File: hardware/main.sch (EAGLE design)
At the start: 97 parts, among them IC1 MPU-6050, IC2 TB6612FNG, Q1 TEFT4300, Q2 TEFT4300, Q3 TEFT4300, Q4 TEFT4300, Q5 TEFT4300, Q6 TEFT4300, Q7 IRLML2244, Q9 IRLML2244, T1 IRLML0030, T2 IRLML0030, T3 IRLML0030, T4 IRLML0030, T5 IRLML0030, T6 IRLML0030, T8 IRLML0030

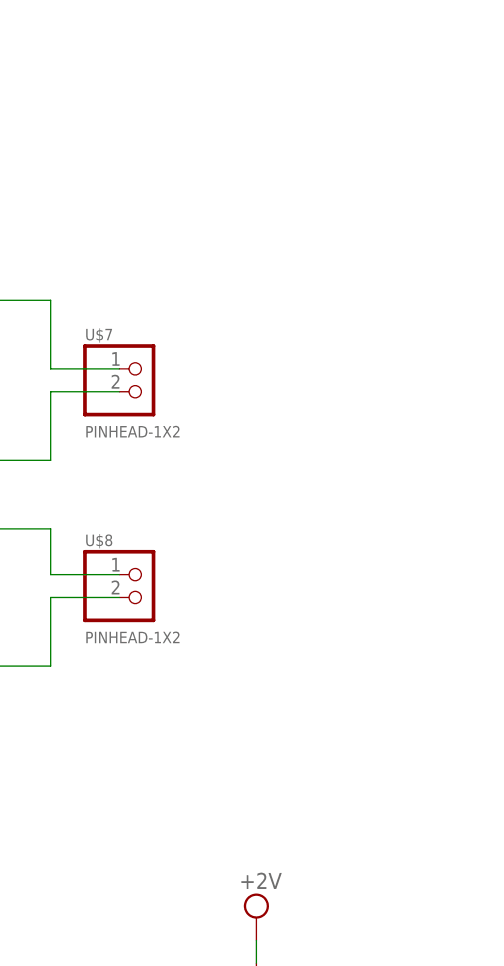
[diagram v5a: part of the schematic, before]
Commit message: added led_mount to model, pcb elemets grouped
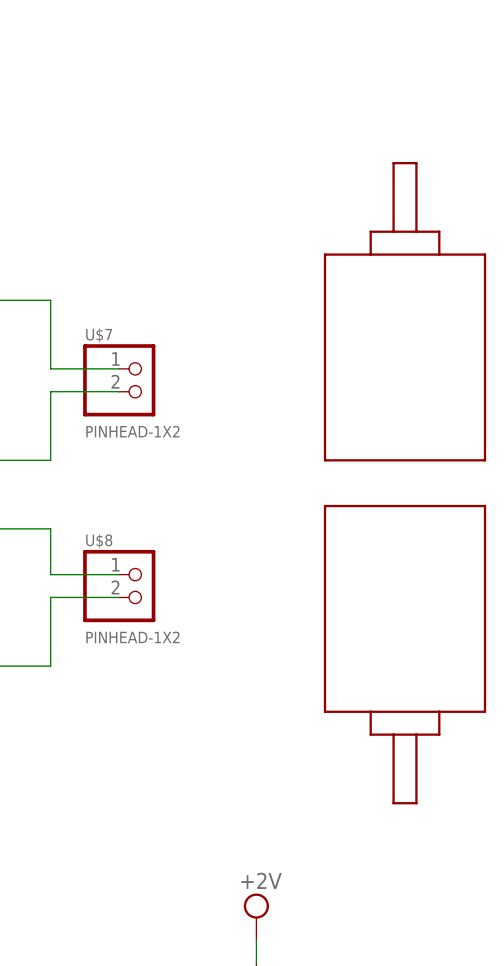
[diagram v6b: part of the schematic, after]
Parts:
- added M1: MOTOR_MOUNT_V2, micromouse:MOTOR_MOUNT_V2
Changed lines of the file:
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@@
 <?xml version="1.0" encoding="utf-8"?>
 <!DOCTYPE eagle SYSTEM "eagle.dtd">
-<eagle version="7.7.0">
+<eagle version="8.0.0">
 <drawing>
 <settings>
@@
 <grid distance="0.1" unitdist="inch" unit="inch" style="lines" multiple="1" display="no" altdistance="0.01" altunitdist="inch" altunit="inch"/>
 <layers>
-<layer number="1" name="Top" color="4" fill="1" visible="yes" active="no"/>
-<layer number="2" name="Route2" color="1" fill="3" visible="yes" active="no"/>
-<layer number="3" name="Route3" color="4" fill="3" visible="yes" active="no"/>
-<layer number="4" name="Route4" color="1" fill="4" visible="yes" active="no"/>
-<layer number="5" name="Route5" color="4" fill="4" visible="yes" active="no"/>
-<layer number="6" name="Route6" color="1" fill="8" visible="yes" active="no"/>
-<layer number="7" name="Route7" color="4" fill="8" visible="yes" active="no"/>
-<layer number="8" name="Route8" color="1" fill="2" visible="yes" active="no"/>
-<layer number="9" name="Route9" color="4" fill="2" visible="yes" active="no"/>
-<layer number="10" name="Route10" color="1" fill="7" visible="yes" active="no"/>
-<layer number="11" name="Route11" color="4" fill="7" visible="yes" active="no"/>
-<layer number="12" name="Route12" color="1" fill="5" visible="yes" active="no"/>
-<layer number="13" name="Route13" color="4" fill="5" visible="yes" active="no"/>
-<layer number="14" name="Route14" color="1" fill="6" visible="yes" active="no"/>
-<layer number="15" name="Route15" color="4" fill="6" visible="yes" active="no"/>
-<layer number="16" name="Bottom" color="1" fill="1" visible="yes" active="no"/>
-<layer number="17" name="Pads" color="2" fill="1" visible="yes" active="no"/>
-<layer number="18" name="Vias" color="2" fill="1" visible="yes" active="no"/>
-<layer number="19" name="Unrouted" color="6" fill="1" visible="yes" active="no"/>
-<layer number="20" name="Dimension" color="15" fill="1" visible="yes" active="no"/>
-<layer number="21" name="tPlace" color="7" fill="1" visible="yes" active="no"/>
-<layer number="22" name="bPlace" color="7" fill="1" visible="yes" active="no"/>
-<layer number="23" name="tOrigins" color="15" fill="1" visible="yes" active="no"/>
-<layer number="24" name="bOrigins" color="15" fill="1" visible="yes" active="no"/>
-<layer number="25" name="tNames" color="7" fill="1" visible="yes" active="no"/>
-<layer number="26" name="bNames" color="7" fill="1" visible="yes" active="no"/>
-<layer number="27" name="tValues" color="7" fill="1" visible="yes" active="no"/>
-<layer number="28" name="bValues" color="7" fill="1" visible="yes" active="no"/>
+<layer number="1" name="Top" color="4" fill="1" visible="no" active="no"/>
+<layer number="2" name="Route2" color="1" fill="3" visible="no" active="no"/>
+<layer number="3" name="Route3" color="4" fill="3" visible="no" active="no"/>
+<layer number="4" name="Route4" color="1" fill="4" visible="no" active="no"/>
+<layer number="5" name="Route5" color="4" fill="4" visible="no" active="no"/>
+<layer number="6" name="Route6" color="1" fill="8" visible="no" active="no"/>
+<layer number="7" name="Route7" color="4" fill="8" visible="no" active="no"/>
+<layer number="8" name="Route8" color="1" fill="2" visible="no" active="no"/>
+<layer number="9" name="Route9" color="4" fill="2" visible="no" active="no"/>
+<layer number="10" name="Route10" color="1" fill="7" visible="no" active="no"/>
+<layer number="11" name="Route11" color="4" fill="7" visible="no" active="no"/>
+<layer number="12" name="Route12" color="1" fill="5" visible="no" active="no"/>
+<layer number="13" name="Route13" color="4" fill="5" visible="no" active="no"/>
+<layer number="14" name="Route14" color="1" fill="6" visible="no" active="no"/>
+<layer number="15" name="Route15" color="4" fill="6" visible="no" active="no"/>
+<layer number="16" name="Bottom" color="1" fill="1" visible="no" active="no"/>
+<layer number="17" name="Pads" color="2" fill="1" visible="no" active="no"/>
+<layer number="18" name="Vias" color="2" fill="1" visible="no" active="no"/>
+<layer number="19" name="Unrouted" color="6" fill="1" visible="no" active="no"/>
+<layer number="20" name="Dimension" color="15" fill="1" visible="no" active="no"/>
+<layer number="21" name="tPlace" color="7" fill="1" visible="no" active="no"/>
+<layer number="22" name="bPlace" color="7" fill="1" visible="no" active="no"/>
+<layer number="23" name="tOrigins" color="15" fill="1" visible="no" active="no"/>
+<layer number="24" name="bOrigins" color="15" fill="1" visible="no" active="no"/>
+<layer number="25" name="tNames" color="7" fill="1" visible="no" active="no"/>
+<layer number="26" name="bNames" color="7" fill="1" visible="no" active="no"/>
+<layer number="27" name="tValues" color="7" fill="1" visible="no" active="no"/>
+<layer number="28" name="bValues" color="7" fill="1" visible="no" active="no"/>
 <layer number="29" name="tStop" color="7" fill="3" visible="no" active="no"/>
 <layer number="30" name="bStop" color="7" fill="6" visible="no" active="no"/>
@@
 <layer number="35" name="tGlue" color="7" fill="4" visible="no" active="no"/>
 <layer number="36" name="bGlue" color="7" fill="5" visible="no" active="no"/>
-<layer number="37" name="tTest" color="7" fill="1" visible="yes" active="no"/>
-<layer number="38" name="bTest" color="7" fill="1" visible="yes" active="no"/>
+<layer number="37" name="tTest" color="7" fill="1" visible="no" active="no"/>
+<layer number="38" name="bTest" color="7" fill="1" visible="no" active="no"/>
 <layer number="39" name="tKeepout" color="4" fill="11" visible="no" active="no"/>
 <layer number="40" name="bKeepout" color="1" fill="11" visible="no" active="no"/>
@@
 <layer number="44" name="Drills" color="7" fill="1" visible="no" active="no"/>
 <layer number="45" name="Holes" color="7" fill="1" visible="no" active="no"/>
-<layer number="46" name="Milling" color="3" fill="1" visible="yes" active="no"/>
-<layer number="47" name="Measures" color="7" fill="1" visible="yes" active="no"/>
-<layer number="48" name="Document" color="7" fill="1" visible="yes" active="no"/>
-<layer number="49" name="Reference" color="7" fill="1" visible="yes" active="no"/>
-<layer number="50" name="dxf" color="7" fill="1" visible="yes" active="no"/>
-<layer number="51" name="tDocu" color="7" fill="1" visible="yes" active="no"/>
-<layer number="52" name="bDocu" color="7" fill="1" visible="yes" active="no"/>
-<layer number="53" name="tGND_GNDA" color="7" fill="9" visible="yes" active="no"/>
-<layer number="54" name="bGND_GNDA" color="1" fill="9" visible="yes" active="no"/>
-<layer number="56" name="wert" color="7" fill="1" visible="yes" active="no"/>
-<layer number="57" name="tCAD" color="7" fill="1" visible="yes" active="no"/>
-<layer number="59" name="tCarbon" color="7" fill="1" visible="yes" active="no"/>
-<layer number="60" name="bCarbon" color="7" fill="1" visible="yes" active="no"/>
+<layer number="46" name="Milling" color="3" fill="1" visible="no" active="no"/>
+<layer number="47" name="Measures" color="7" fill="1" visible="no" active="no"/>
+<layer number="48" name="Document" color="7" fill="1" visible="no" active="no"/>
+<layer number="49" name="Reference" color="7" fill="1" visible="no" active="no"/>
+<layer number="50" name="dxf" color="7" fill="1" visible="no" active="no"/>
+<layer number="51" name="tDocu" color="7" fill="1" visible="no" active="no"/>
+<layer number="52" name="bDocu" color="7" fill="1" visible="no" active="no"/>
+<layer number="53" name="tGND_GNDA" color="7" fill="9" visible="no" active="no"/>
+<layer number="54" name="bGND_GNDA" color="1" fill="9" visible="no" active="no"/>
+<layer number="56" name="wert" color="7" fill="1" visible="no" active="no"/>
+<layer number="57" name="tCAD" color="7" fill="1" visible="no" active="no"/>
+<layer number="59" name="tCarbon" color="7" fill="1" visible="no" active="no"/>
+<layer number="60" name="bCarbon" color="7" fill="1" visible="no" active="no"/>
 <layer number="90" name="Modules" color="5" fill="1" visible="yes" active="yes"/>
 <layer number="91" name="Nets" color="2" fill="1" visible="yes" active="yes"/>
@@
 <part name="R3_1" library="rcl" deviceset="R-EU_" device="R0603" value="10k"/>
 <part name="R3_2" library="rcl" deviceset="R-EU_" device="R0603" value="10k"/>
+<part name="M1" library="micromouse" deviceset="MOTOR_MOUNT_V2" device=""/>
 </parts>
 <sheets>
@@
 <instance part="R3_1" gate="G$1" x="-104.14" y="170.18" rot="R180"/>
 <instance part="R3_2" gate="G$1" x="-104.14" y="124.46" rot="R180"/>
+<instance part="M1" gate="G$1" x="182.88" y="294.64"/>
 </instances>
 <busses>

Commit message: power supply layout almost done
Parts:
- removed SW2, SW3, SW4: (no value), BaseApp:TACTILE-2PIN
- removed U$2, U$3: PINHEAD-1X2, BaseApp:PINHEAD-1X2
- added C_V4: 100n, rcl:C-EUC0603
- added D9: transil, nxp_60:BAS321
- added JP1, JP2: (no value), SparkFun_conn:M02POLAR
- added LED1: red, led:LEDSML1206
- added LED2: green, led:LEDSML1206
- added LED3: yellow, led:LEDSML1206
- added LED4, LED6: blue, led:LEDSML1206
- added R26, R27, R28: 150R, resistor:R-EU_R0805
- added R29, R33: 33R, resistor:R-EU_R0805
- added S1, S3, S4: (no value), EAGLE-TACT_SWITCHES-rev17c:434153017835
- added S2: (no value), EAGLE-TACT_SWITCHES-rev17c:450301014042
- C5: device rcl:C-EUC1206 -> rcl:C-EUC0603
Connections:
- removed net N$41: U$2.2, U$3.1
- removed net VM: C6.2, C7.2, IC2.VM1, IC2.VM2, IC2.VM3
- new net LED2: LED2.C
- new net LED3: LED3.C
- new net LED4: LED4.C
- new net LED5: LED6.C
- new net N$19: JP1.1, JP2.2
- new net N$20: LED1.A, R26.1
- new net N$21: LED2.A, R27.1
- new net N$22: LED3.A, R28.1
- new net N$24: LED4.A, R29.1
- new net N$25: LED6.A, R33.1
- net +3V3: now also C_V4.1, R26.2, R27.2, R28.2, R29.2, R33.2, S1.4; no longer SW3.1
- net +7V: now also C6.2, C7.2, D9.K, IC2.VM1, IC2.VM2, IC2.VM3
- net BTN1: no longer SW2.1
- net GND: now also C_V4.2, JP2.1, LED1.C; no longer SW4.1, U$2.1
- net GNDA: now also D9.A
- net N$2: now also S4.4; no longer SW2.2
- net N$23: now also S1.1; no longer SW3.2
- net N$43: now also Q7.S; no longer U$3.2
- net N$46: now also JP1.2; no longer Q7.S
- net RST: now also S3.4; no longer SW4.2
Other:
- note added: "GRM188R61C106MA73D"
- moved on the sheet: C_V1, C_V2, C_V3, VCAP_1, VCAP_2

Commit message: pcb 29.06
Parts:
- removed D1, D2, D3, D4, D5, D7: SFH4545-C, _microMouse:SFH4545-C
- removed Q1, Q2, Q3, Q4, Q5, Q6: TEFT4300, _MM:TEFT4300
- added L1: LABITYNT, micromouse:LABITYNT
- added M2, M3, M4, M5, M6, M7: LED_MOUNT, micromouse:LED_MOUNT
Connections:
- removed net ENCLB: U$6.PA1
- removed net USART1_RX: SV1.6, U$6.PB7
- removed net USART1_TX: SV1.8, U$6.PB6
- new net USART3_RX: SV1.6, U$6.PB11
- new net USART3_TX: SV1.8, U$6.PB10
- net +3V3: now also M2Q.C, M3Q.C, M4Q.C, M5Q.C, M6Q.C, M7Q.C; no longer Q1.C, Q2.C, Q3.C, Q4.C, Q5.C, Q6.C
- net ADC_L: now also M7Q.E; no longer Q3.E
- net ADC_LF: now also M2Q.E; no longer Q2.E
- net ADC_LS: now also M3Q.E; no longer Q1.E
- net ADC_R: now also M6Q.E; no longer Q4.E
- net ADC_RF: now also M5Q.E; no longer Q5.E
- net ADC_RS: now also M4Q.E; no longer Q6.E
- net DIV_EN: no longer U$6.PB10
- net ENCL_B: now also U$6.PA1
- net LED2: now also U$6.PC10
- net LED3: now also U$6.PC11
- net ML_IN1: now also U$6.PC7; no longer U$6.PC6
- net ML_IN2: now also U$6.PC6; no longer U$6.PC7
- net N$1: now also M3D.C; no longer D1.C
- net N$10: now also M6D.C; no longer D4.C
- net N$12: now also M7D.C; no longer D5.C
- net N$3: now also M2D.C; no longer D7.C
- net N$6: now also M4D.C; no longer D2.C
- net N$8: now also M5D.C; no longer D3.C
- net SPI2_CS2: now also U$6.PB4; no longer U$6.PB11
- net VCC: now also M2D.A, M3D.A, M4D.A, M5D.A, M6D.A, M7D.A; no longer D1.A, D2.A, D3.A, D4.A, D5.A, D7.A
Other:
- moved on the sheet: R23, R24, R30, R31
